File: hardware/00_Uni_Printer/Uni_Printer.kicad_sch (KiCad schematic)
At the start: 64 parts, among them J1 Conn_01x04_Male, J2 FIDUCIAL, J4 Conn_01x06, J5 Conn_02x10_Odd_Even, J6 Conn_02x10_Odd_Even, J6 FIDUCIAL, J7 Conn_02x10_Odd_Even, J8 Conn_02x10_Odd_Even, U2 74AHC04, U3 74AHC04, U6 LM2904

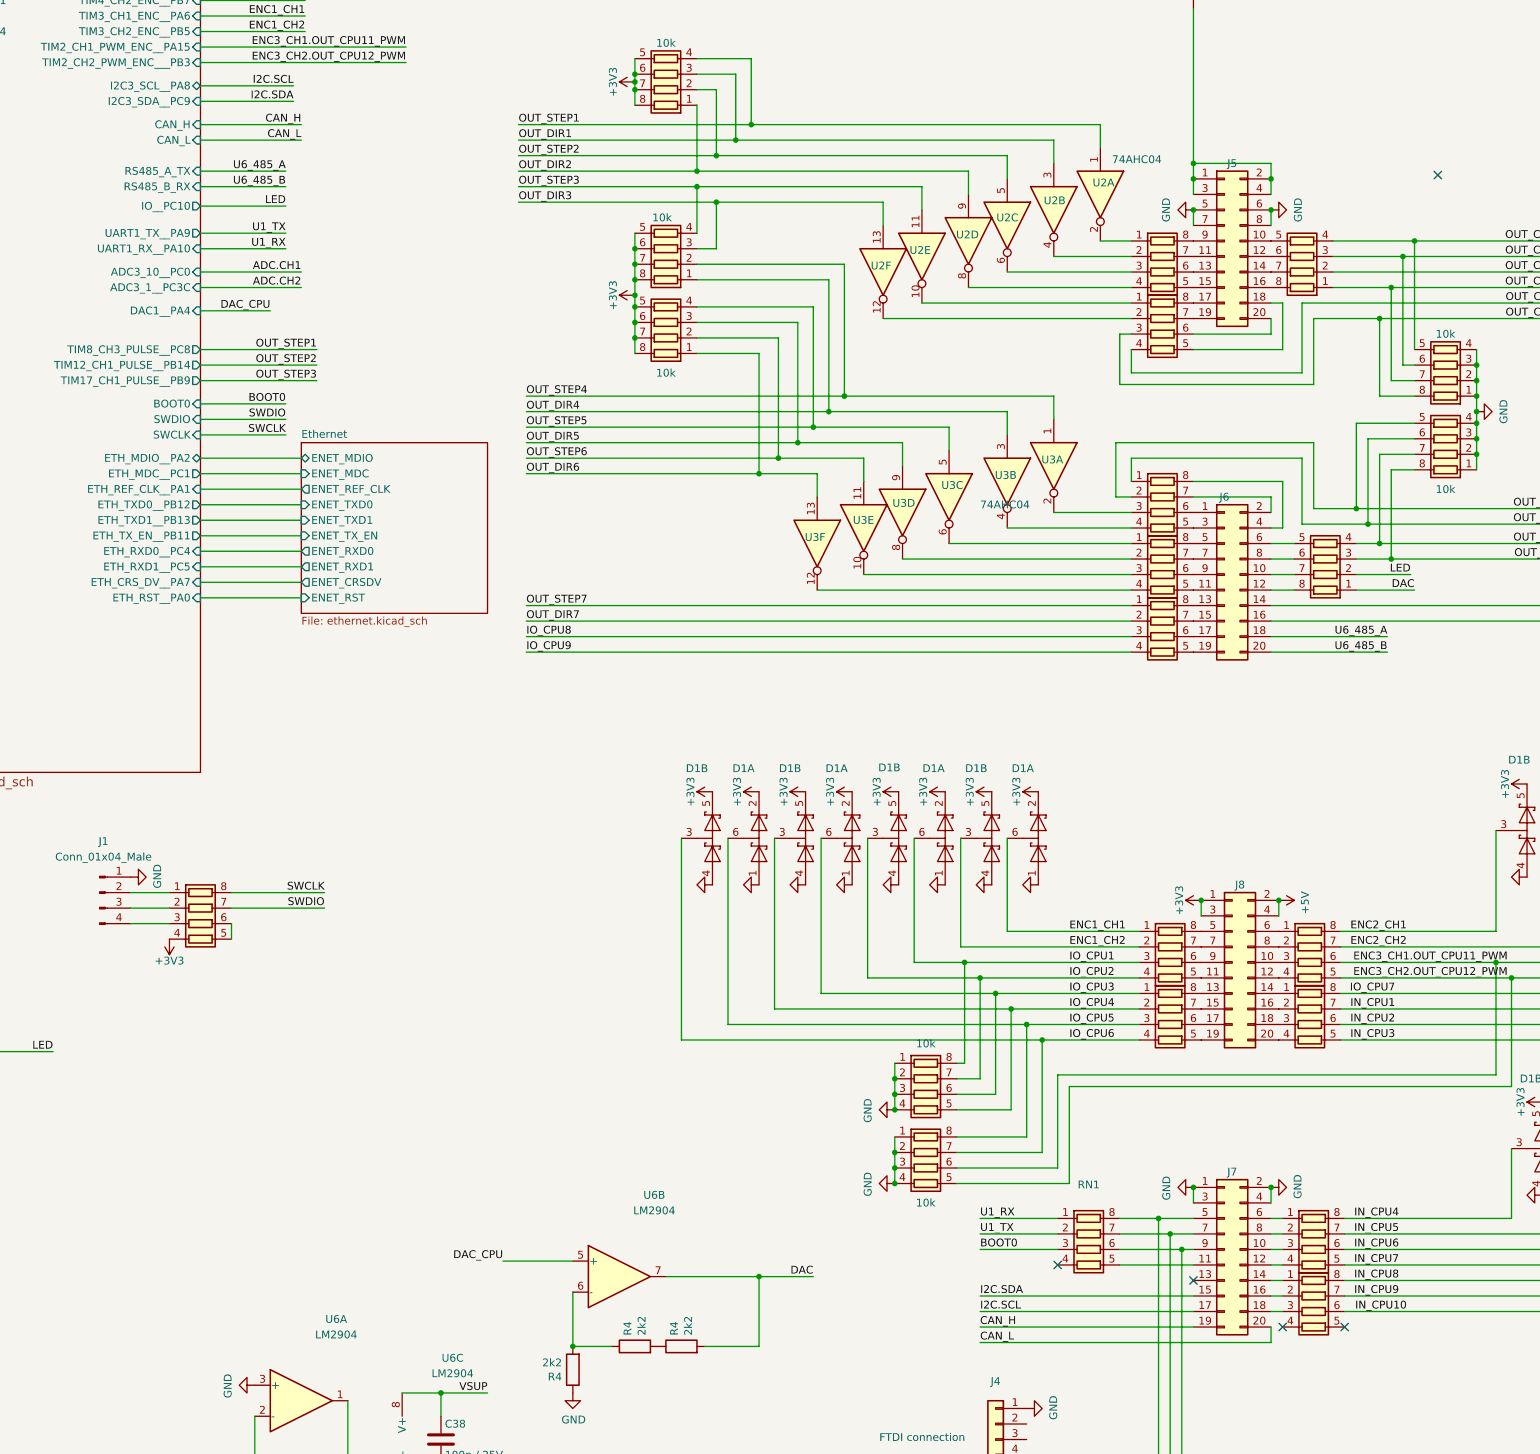
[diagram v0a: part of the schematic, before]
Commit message: Removed CAN and RS485 drivers
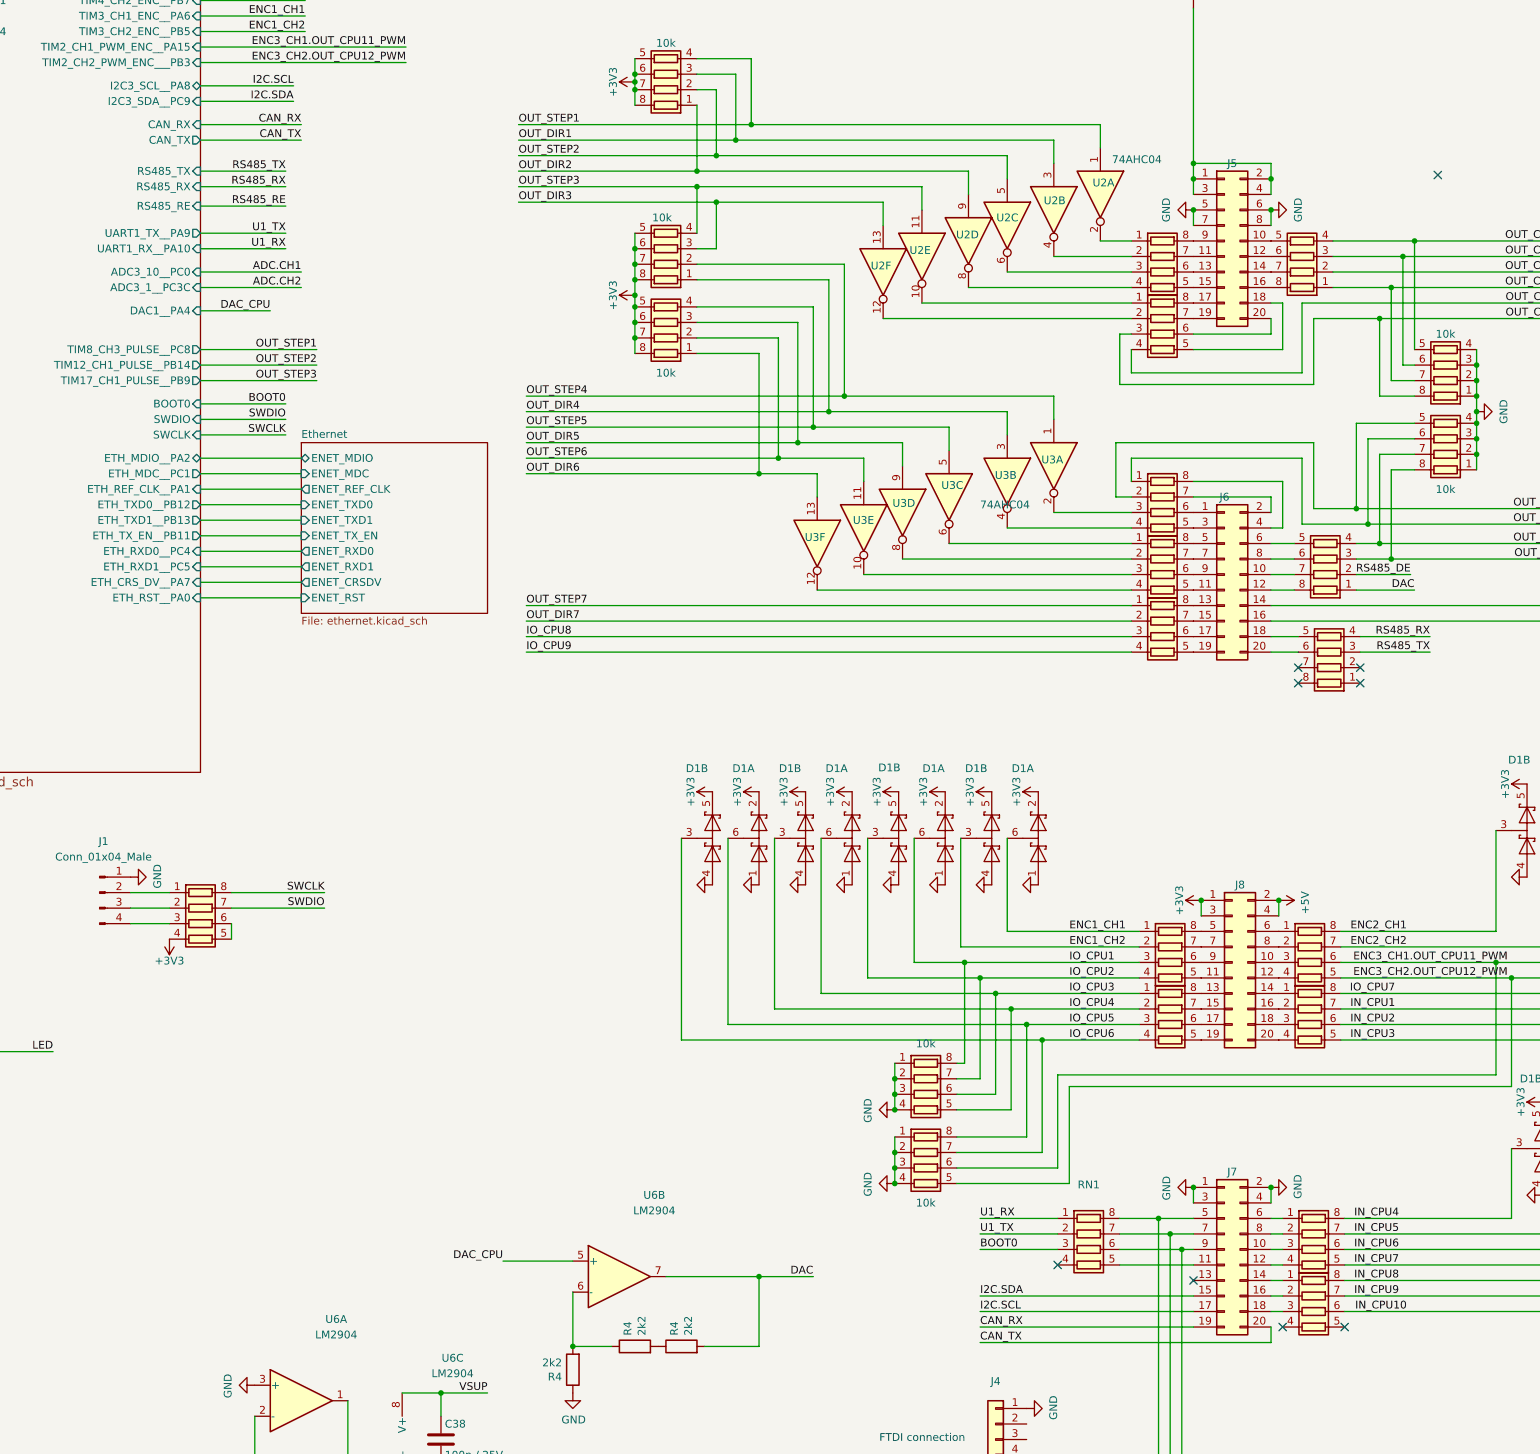
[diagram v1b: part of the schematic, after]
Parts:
- added RN6: 100R, moje:R_Array_Convex_4x0603, symbol Device:R_Pack04
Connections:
- net LED: no longer RN6.2 (R2.1)
- net CAN_H renamed CAN_RX
- net CAN_L renamed CAN_TX
- net U6_485_A: no longer names the net of J6.18 (Pin_18)
- net U6_485_A: now also RN6.5 (R4.2)
- net U6_485_B: no longer names the net of J6.20 (Pin_20)
- net U6_485_B: now also RN6.6 (R3.2)
- new net RS485_DE: RN6.2 (R2.1)
- new net RS485_RX: RN6.4 (R4.1)
- new net RS485_TX: RN6.3 (R3.1)
- no-connect marks 7 -> 11
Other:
- sheet Processor ports: added CAN_RX, CAN_TX, RS485_RE, RS485_RX, RS485_TX; removed CAN_H, CAN_L, IO__PC10, RS485_A_TX, RS485_B_RX

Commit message: Fixes in PCB design
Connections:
- net RS485_DE is gone; now on net RS485_RE: RN6.2 (R2.1)
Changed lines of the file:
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@@
     (effects (font (size 1.27 1.27)) (justify left bottom))
   )
-  (label "RS485_DE" (at 303.53 124.46 180)
+  (label "RS485_RE" (at 303.53 124.46 180)
     (effects (font (size 1.27 1.27)) (justify right bottom))
   )
@@
       (reference "#PWR0101") (unit 1) (value "GND-Sensor_tank_v1-rescue-Uni_General_v1-rescue-Uni_Printer_v1-rescue") (footprint "")
     )
-    (path "/00000000-0000-0000-0000-00005c984242/e9aaa5ad-afec-4745-8ff5-83406401d3a1"
-      (reference "#PWR0102") (unit 1) (value "GND") (footprint "")
-    )
-    (path "/00000000-0000-0000-0000-00005c984242/cbc659df-d4a7-4995-afd7-19644ec0137f"
-      (reference "#PWR0103") (unit 1) (value "+3V3") (footprint "")
-    )
     (path "/4be14d84-8cd4-4ecd-812a-0214e5e58c67"
       (reference "#PWR0104") (unit 1) (value "+3V3") (footprint "")
@@
       (reference "#PWR0105") (unit 1) (value "GND-Sensor_tank_v1-rescue-Uni_General_v1-rescue-Uni_Printer_v1-rescue") (footprint "")
     )
-    (path "/00000000-0000-0000-0000-00005c984242/257c531d-611b-427c-ae52-5178706d70ab"
-      (reference "#PWR0106") (unit 1) (value "+3V3") (footprint "")
-    )
     (path "/e91f46bd-d7d5-4b14-8252-46dcba475b09"
       (reference "#PWR0108") (unit 1) (value "+3V3") (footprint "")
@@
       (reference "C31") (unit 1) (value "100n") (footprint "Capacitor_SMD:C_0603_1608Metric")
     )
-    (path "/00000000-0000-0000-0000-00005c984242/450ce09e-f005-4b3c-bec6-61e07a176932"
-      (reference "C32") (unit 1) (value "100n / 25V") (footprint "Capacitor_SMD:C_0603_1608Metric")
-    )
     (path "/19e3c943-ba04-4ec6-bbe1-e9e8a6d18ef5"

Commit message: Prepared for first prototype
Signed-off-by: Jarosław Karwik <jaroslaw.karwik@gmail.com>
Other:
- sheet Processor ports: added IO__PC10; removed none
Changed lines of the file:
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@@
     (stroke (width 0) (type default) (color 0 0 0 0))
   )
+  (wire (pts (xy 105.41 83.82) (xy 116.84 83.82))
+    (stroke (width 0) (type default) (color 0 0 0 0))
+  )
   (wire (pts (xy 398.78 63.5) (xy 398.78 52.07))
     (stroke (width 0) (type default) (color 0 0 0 0))
@@
     (effects (font (size 1.27 1.27)) (justify left bottom))
   )
+  (label "LED" (at 116.84 83.82 0) (fields_autoplaced)
+    (effects (font (size 1.27 1.27)) (justify right bottom))
+  )
   (label "OUT_STEP6" (at 158.75 105.41 0) (fields_autoplaced)
     (effects (font (size 1.27 1.27)) (justify left bottom))
@@
       (effects (font (size 1.27 1.27)) (justify right))
     )
+    (pin "IO__PC10" output (at 105.41 83.82 0)
+      (effects (font (size 1.27 1.27)) (justify right))
+    )
